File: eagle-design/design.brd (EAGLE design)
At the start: 83.8 x 51.7 mm, 19 parts, among them J1 61300411121, J2 10103594, U1 ATMEGA328P-AU

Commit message: Updated design and export files
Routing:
- net GND: track 192.7 -> 176.9 mm
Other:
- board text added: "CAD Engineer | DevOps Engineer Hardware Developer | Open Source Developer"
- board text removed: "DevOps Engineer | Hardware Developer Open Source Developer"
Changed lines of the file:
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@@
 <dimension x1="2.3114" y1="52.6544" x2="2.3114" y2="0.9144" x3="-8.89" y3="26.7844" textsize="1.778" layer="1"/>
 <dimension x1="2.3114" y1="0.9144" x2="86.1114" y2="0.9144" x3="44.2114" y3="-11.43" textsize="1.778" layer="1"/>
-<text x="37.8714" y="41.5544" size="6.35" layer="29">Sashwat K</text>
-<wire x1="39.1414" y1="40.2844" x2="81.0514" y2="40.2844" width="0.8128" layer="29"/>
-<text x="37.8714" y="33.9344" size="1.778" layer="29">DevOps Engineer | Hardware Developer
-         Open Source Developer</text>
+<text x="37.0332" y="41.402" size="6.35" layer="29">Sashwat K</text>
+<wire x1="36.322" y1="40.0558" x2="81.1276" y2="40.0558" width="0.8128" layer="29"/>
+<text x="33.0708" y="34.2392" size="1.778" layer="29">          CAD Engineer | DevOps Engineer
+Hardware Developer | Open Source Developer</text>
 <text x="82.6262" y="50.4444" size="1.27" layer="22" rot="MR0">Business Card</text>
 <text x="49.6824" y="24.9174" size="1.905" layer="29">- sashwat.in
@@
 <wire x1="45.9814" y1="11.4744" x2="42.0814" y2="11.4744" width="0.4572" layer="1"/>
 <wire x1="42.0814" y1="11.4744" x2="41.2814" y2="10.6744" width="0.4572" layer="1"/>
-<wire x1="40.6314" y1="28.8544" x2="40.6314" y2="26.3144" width="0.4572" layer="1"/>
+<wire x1="40.6314" y1="28.8544" x2="40.6314" y2="28.8036" width="0.4572" layer="1"/>
+<wire x1="40.6314" y1="28.8036" x2="40.6314" y2="26.3144" width="0.4572" layer="1"/>
 <wire x1="45.9814" y1="11.4744" x2="47.1614" y2="11.4744" width="0.4572" layer="1"/>
 <wire x1="47.1614" y1="11.4744" x2="48.0314" y2="12.3444" width="0.4572" layer="1"/>
@@
 <wire x1="41.6814" y1="31.3944" x2="40.6314" y2="30.3444" width="0.4572" layer="1"/>
 <wire x1="40.6314" y1="30.3444" x2="40.6314" y2="28.8544" width="0.4572" layer="1"/>
-<wire x1="15.0114" y1="49.1744" x2="15.0114" y2="49.6572" width="0.4572" layer="1"/>
-<wire x1="15.0114" y1="49.6572" x2="16.2814" y2="50.9272" width="0.4572" layer="1"/>
-<wire x1="16.2814" y1="50.9272" x2="32.9436" y2="50.9272" width="0.4572" layer="1"/>
-<wire x1="32.9436" y1="50.9272" x2="34.0614" y2="49.8094" width="0.4572" layer="1"/>
-<wire x1="34.0614" y1="49.8094" x2="34.0614" y2="27.5844" width="0.4572" layer="1"/>
-<wire x1="34.0614" y1="27.5844" x2="35.3314" y2="26.3144" width="0.4572" layer="1"/>
-<wire x1="35.3314" y1="26.3144" x2="40.6314" y2="26.3144" width="0.4572" layer="1"/>
+<wire x1="15.0114" y1="49.1744" x2="26.2255" y2="37.9603" width="0.4572" layer="1"/>
 <via x="53.1114" y="13.6144" extent="1-16" drill="0.35"/>
 <via x="49.9364" y="13.6144" extent="1-16" drill="0.35"/>
+<wire x1="26.2255" y1="37.9603" x2="26.3905" y2="37.7953" width="0.4572" layer="1"/>
 <wire x1="49.9364" y1="13.6144" x2="53.1114" y2="13.6144" width="0.4572" layer="16"/>
 <wire x1="48.0314" y1="12.3444" x2="48.6664" y2="12.3444" width="0.4572" layer="1"/>
@@
 <wire x1="17.8714" y1="8.8494" x2="17.5514" y2="9.1694" width="0.4572" layer="1"/>
 <wire x1="17.5514" y1="12.9794" x2="17.5514" y2="9.1694" width="0.4572" layer="16"/>
+<wire x1="26.3905" y1="37.7953" x2="35.3822" y2="28.8036" width="0.4572" layer="1"/>
+<wire x1="35.3822" y1="28.8036" x2="40.6314" y2="28.8036" width="0.4572" layer="1"/>
 <wire x1="37.3814" y1="10.6744" x2="37.3814" y2="12.2744" width="0" layer="19" extent="1-1"/>
 </signal>

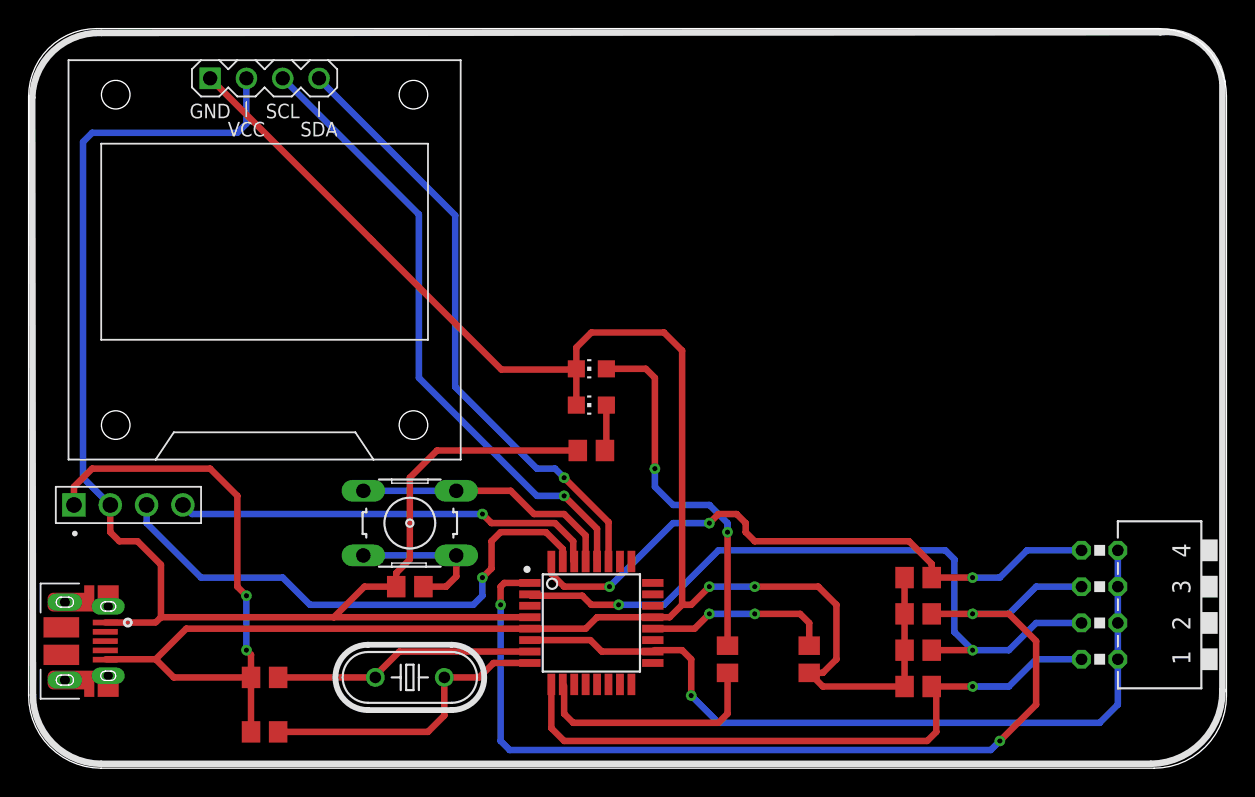
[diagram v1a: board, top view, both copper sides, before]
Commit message: Added GND plane for bottom layer
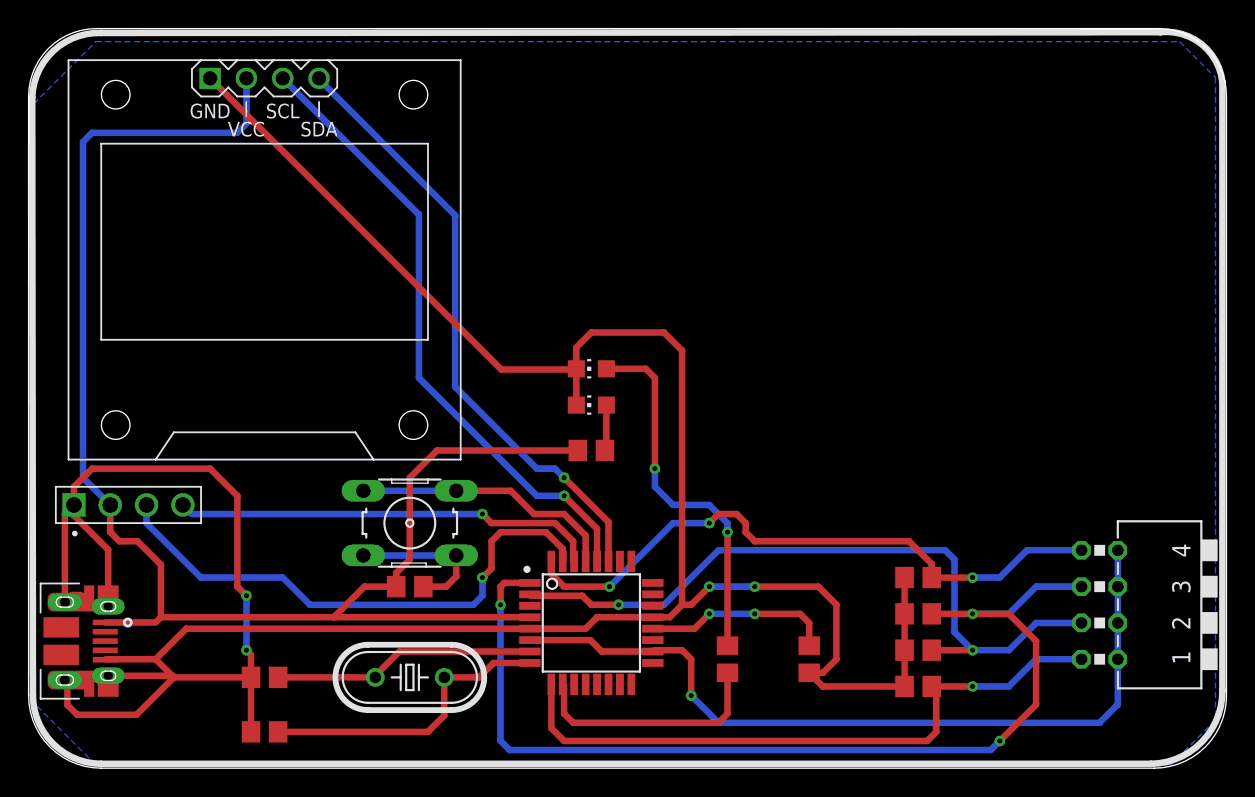
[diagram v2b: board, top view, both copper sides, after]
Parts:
- R3: value (none) -> 10K
- R4, R5, R6, R7: value 220Ω -> 10K
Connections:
- net GND: now also J2.SH1, J2.SH2, J2.SH3, J2.SH4
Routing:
- net GND: track 176.9 -> 208.4 mm
- added copper zone on layer 16, net GND
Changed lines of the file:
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@@
 <element name="R1" library="resistor" library_urn="urn:adsk.eagle:library:348" package="R0805" package3d_urn="urn:adsk.eagle:package:23553/2" value="220Ω" x="51.2064" y="8.5344" smashed="yes" rot="R90"/>
 <element name="R2" library="resistor" library_urn="urn:adsk.eagle:library:348" package="R0805" package3d_urn="urn:adsk.eagle:package:23553/2" value="220Ω" x="41.6814" y="23.1394" smashed="yes"/>
-<element name="R3" library="resistor" library_urn="urn:adsk.eagle:library:348" package="R0805" package3d_urn="urn:adsk.eagle:package:23553/2" value="" x="28.9814" y="13.6144" smashed="yes">
-<attribute name="VALUE" x="28.3464" y="11.0744" size="1.27" layer="27"/>
-</element>
-<element name="R4" library="resistor" library_urn="urn:adsk.eagle:library:348" package="R0805" package3d_urn="urn:adsk.eagle:package:23553/2" value="220Ω" x="64.5414" y="14.2494" smashed="yes"/>
-<element name="R5" library="resistor" library_urn="urn:adsk.eagle:library:348" package="R0805" package3d_urn="urn:adsk.eagle:package:23553/2" value="220Ω" x="64.5414" y="11.7094" smashed="yes"/>
-<element name="R6" library="resistor" library_urn="urn:adsk.eagle:library:348" package="R0805" package3d_urn="urn:adsk.eagle:package:23553/2" value="220Ω" x="64.5414" y="9.1694" smashed="yes"/>
-<element name="R7" library="resistor" library_urn="urn:adsk.eagle:library:348" package="R0805" package3d_urn="urn:adsk.eagle:package:23553/2" value="220Ω" x="64.5414" y="6.6294" smashed="yes"/>
+<element name="R3" library="resistor" library_urn="urn:adsk.eagle:library:348" package="R0805" package3d_urn="urn:adsk.eagle:package:23553/2" value="10K" x="28.9814" y="13.6144" smashed="yes"/>
+<element name="R4" library="resistor" library_urn="urn:adsk.eagle:library:348" package="R0805" package3d_urn="urn:adsk.eagle:package:23553/2" value="10K" x="64.5414" y="14.2494" smashed="yes"/>
+<element name="R5" library="resistor" library_urn="urn:adsk.eagle:library:348" package="R0805" package3d_urn="urn:adsk.eagle:package:23553/2" value="10K" x="64.5414" y="11.7094" smashed="yes"/>
+<element name="R6" library="resistor" library_urn="urn:adsk.eagle:library:348" package="R0805" package3d_urn="urn:adsk.eagle:package:23553/2" value="10K" x="64.5414" y="9.1694" smashed="yes"/>
+<element name="R7" library="resistor" library_urn="urn:adsk.eagle:library:348" package="R0805" package3d_urn="urn:adsk.eagle:package:23553/2" value="10K" x="64.5414" y="6.6294" smashed="yes"/>
 <element name="S1" library="switch-omron" library_urn="urn:adsk.eagle:library:377" package="B3F-10XX" package3d_urn="urn:adsk.eagle:package:27496/1" value="" x="28.9814" y="18.0594" smashed="yes">
 <attribute name="MF" value="" x="75.9714" y="-21.3106" size="1.778" layer="27" display="off"/>
@@
 <signal name="GND">
 <contactref element="J1" pad="1"/>
-<contactref element="J2" pad="5"/>
 <contactref element="U$1" pad="1"/>
 <contactref element="UNLOCK_LED" pad="C"/>
@@
 <contactref element="U1" pad="21"/>
 <wire x1="17.8714" y1="3.4544" x2="17.8714" y2="7.2644" width="0.4572" layer="1"/>
-<wire x1="7.6764" y1="8.5044" x2="7.7064" y2="8.5344" width="0.1524" layer="1"/>
 <wire x1="7.7064" y1="8.5344" x2="11.2014" y2="8.5344" width="0.4572" layer="1"/>
-<wire x1="11.2014" y1="8.5344" x2="12.4714" y2="7.2644" width="0.4572" layer="1"/>
+<wire x1="11.2014" y1="8.5344" x2="12.3564" y2="7.3794" width="0.4572" layer="1"/>
 <wire x1="12.4714" y1="7.2644" x2="17.8714" y2="7.2644" width="0.4572" layer="1"/>
 <wire x1="37.3814" y1="10.6744" x2="13.3414" y2="10.6744" width="0.4572" layer="1"/>
@@
 <wire x1="41.6814" y1="31.3944" x2="40.6314" y2="30.3444" width="0.4572" layer="1"/>
 <wire x1="40.6314" y1="30.3444" x2="40.6314" y2="28.8544" width="0.4572" layer="1"/>
-<wire x1="15.0114" y1="49.1744" x2="26.2255" y2="37.9603" width="0.4572" layer="1"/>
+<wire x1="15.0114" y1="49.1744" x2="35.3822" y2="28.8036" width="0.4572" layer="1"/>
 <via x="53.1114" y="13.6144" extent="1-16" drill="0.35"/>
 <via x="49.9364" y="13.6144" extent="1-16" drill="0.35"/>
-<wire x1="26.2255" y1="37.9603" x2="26.3905" y2="37.7953" width="0.4572" layer="1"/>
 <wire x1="49.9364" y1="13.6144" x2="53.1114" y2="13.6144" width="0.4572" layer="16"/>
 <wire x1="48.0314" y1="12.3444" x2="48.6664" y2="12.3444" width="0.4572" layer="1"/>
@@
 <wire x1="17.8714" y1="8.8494" x2="17.5514" y2="9.1694" width="0.4572" layer="1"/>
 <wire x1="17.5514" y1="12.9794" x2="17.5514" y2="9.1694" width="0.4572" layer="16"/>
-<wire x1="26.3905" y1="37.7953" x2="35.3822" y2="28.8036" width="0.4572" layer="1"/>
 <wire x1="35.3822" y1="28.8036" x2="40.6314" y2="28.8036" width="0.4572" layer="1"/>
+<contactref element="J2" pad="SH1"/>
+<contactref element="J2" pad="SH4"/>
+<contactref element="J2" pad="SH3"/>
+<contactref element="J2" pad="SH2"/>
+<contactref element="J2" pad="5"/>
+<wire x1="4.8514" y1="12.5294" x2="5.3522" y2="13.0302" width="0.4572" layer="1"/>
+<wire x1="5.3522" y1="13.0302" x2="5.9436" y2="13.0302" width="0.4572" layer="1"/>
+<wire x1="4.8514" y1="12.5294" x2="4.8514" y2="18.6944" width="0.4572" layer="1"/>
+<wire x1="4.8514" y1="18.6944" x2="5.4864" y2="19.3294" width="0.4572" layer="1"/>
+<wire x1="7.8814" y1="12.2294" x2="7.8814" y2="16.1978" width="0.4572" layer="1"/>
+<wire x1="5.4864" y1="18.5928" x2="5.4864" y2="19.3294" width="0.4572" layer="1"/>
+<wire x1="7.8814" y1="16.1978" x2="5.4864" y2="18.5928" width="0.4572" layer="1"/>
+<wire x1="7.8814" y1="7.3794" x2="12.3564" y2="7.3794" width="0.4572" layer="1"/>
+<wire x1="12.3564" y1="7.3794" x2="12.4714" y2="7.2644" width="0.4572" layer="1"/>
+<wire x1="4.8514" y1="7.0794" x2="5.0292" y2="6.9016" width="0.4572" layer="1"/>
+<wire x1="5.0292" y1="6.9016" x2="5.0292" y2="5.334" width="0.4572" layer="1"/>
+<wire x1="5.0292" y1="5.334" x2="5.715" y2="4.6482" width="0.4572" layer="1"/>
+<wire x1="9.8552" y1="4.6482" x2="12.4714" y2="7.2644" width="0.4572" layer="1"/>
+<wire x1="5.715" y1="4.6482" x2="9.8552" y2="4.6482" width="0.4572" layer="1"/>
+<polygon width="0.4572" layer="16">
+<vertex x="7.0104" y="51.7398"/>
+<vertex x="82.8294" y="51.7398"/>
+<vertex x="85.344" y="49.2252"/>
+<vertex x="85.344" y="4.2672"/>
+<vertex x="82.2198" y="1.143"/>
+<vertex x="7.0104" y="1.143"/>
+<vertex x="2.667" y="5.4864"/>
+<vertex x="2.667" y="47.3964"/>
+</polygon>
 <wire x1="37.3814" y1="10.6744" x2="37.3814" y2="12.2744" width="0" layer="19" extent="1-1"/>
+<wire x1="7.6764" y1="8.5044" x2="7.7064" y2="8.5344" width="0" layer="19" extent="1-1"/>
 </signal>
 <signal name="5V">
